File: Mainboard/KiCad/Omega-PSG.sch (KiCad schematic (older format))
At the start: 14 parts, among them J7 JOYSTICK_A, J8 JOYSTICK_B, U28 74HCT157, U29 74HCT157, U35 74HCT74, U36 74HCT74, U39 74AHCT32, U4 YM2149, U42 74LS07, U44 74AHCT02

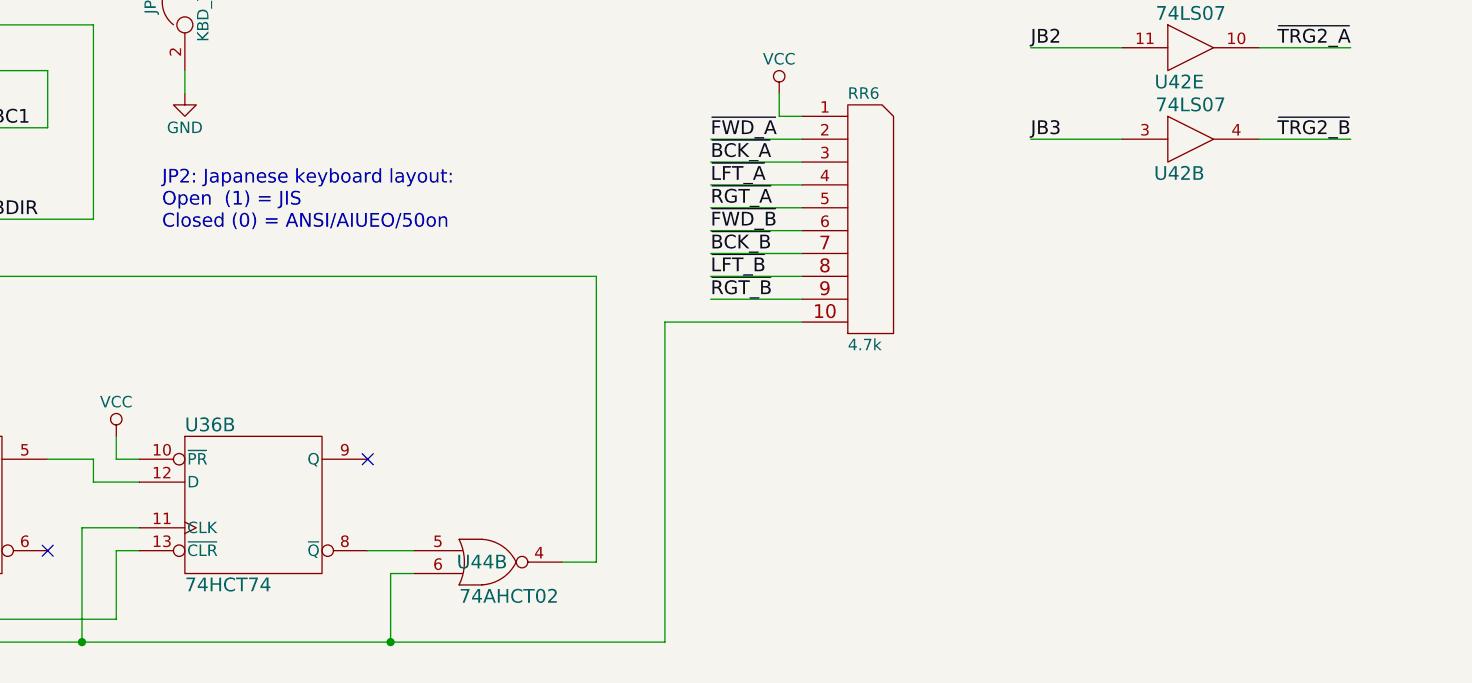
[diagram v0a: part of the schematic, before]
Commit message: Mainboard: Update to version 1.0
Signed-off-by: Sergey Kiselev <skiselev@gmail.com>
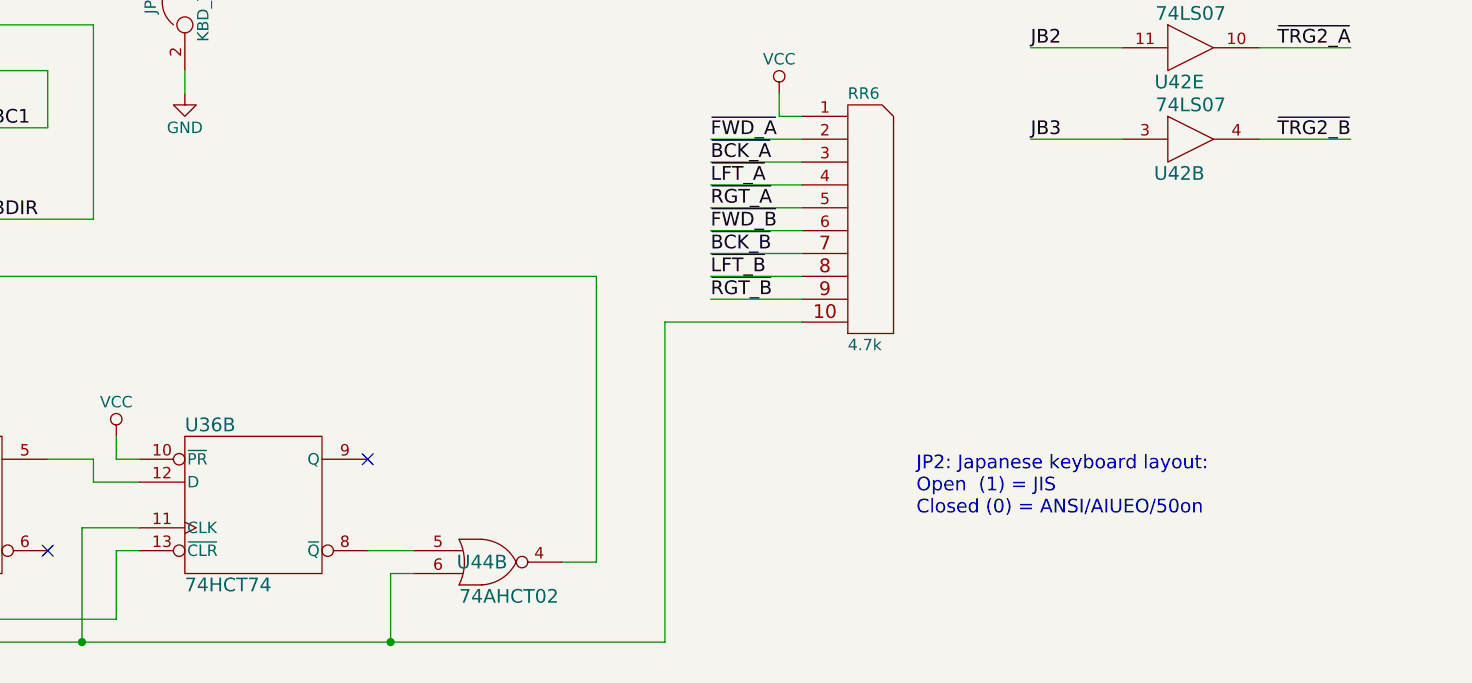
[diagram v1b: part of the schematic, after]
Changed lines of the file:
@@
 	1    0    0    -1
 $EndComp
-Text Notes 3700 5600 0    60   ~ 0
+Text Notes 7000 6850 0    60   ~ 0
 JP2: Japanese keyboard layout:\nOpen  (1) = JIS\nClosed (0) = ANSI/AIUEO/50on
 $Comp

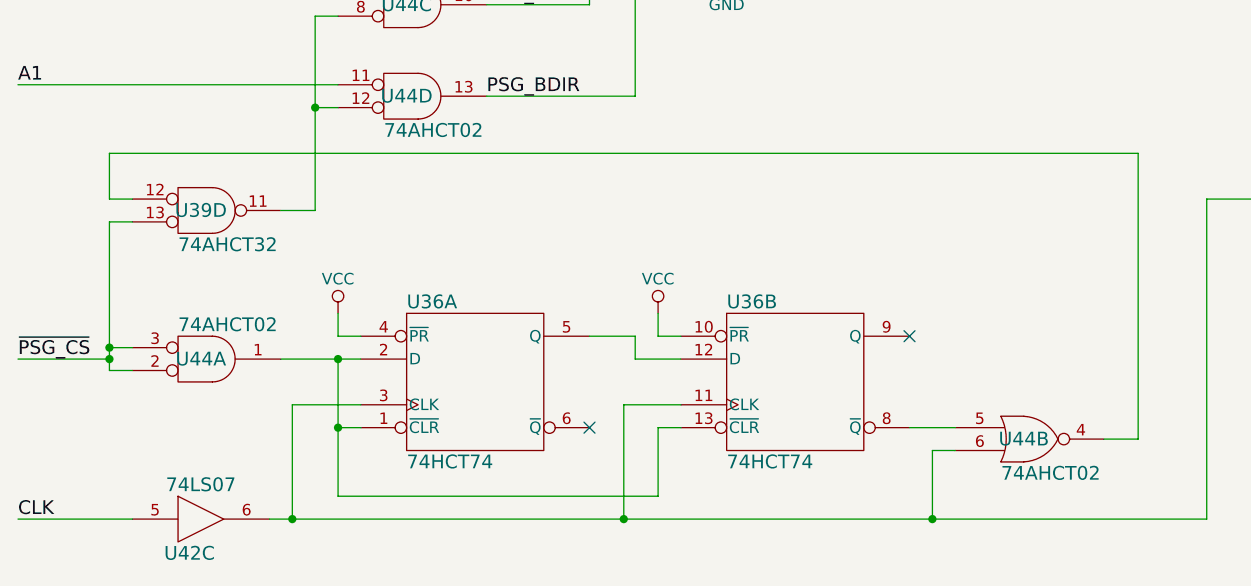
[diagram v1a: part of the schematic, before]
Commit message: Mainboard: Fix the issues discovered so far
Signed-off-by: Sergey Kiselev <skiselev@gmail.com>
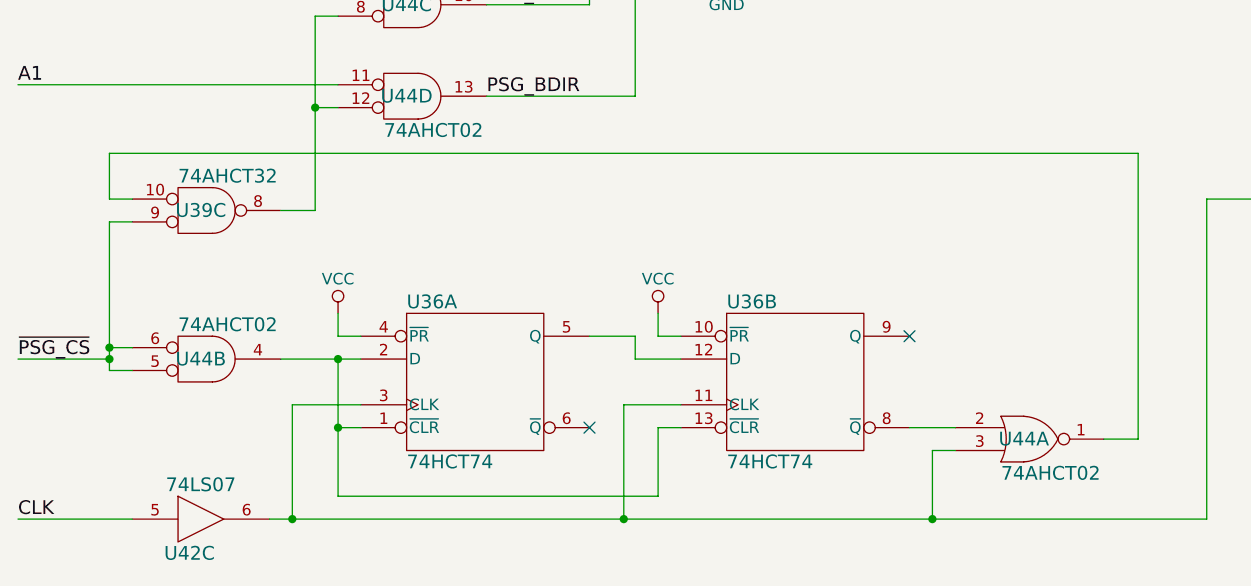
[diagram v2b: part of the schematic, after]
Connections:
- net ~PSG_CS: now also U39.9, U44.5, U44.6; no longer U39.13, U44.2, U44.3
- net at RR6.10, U36.11 (CLK), U36.3 (CLK)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: now also U44.3; no longer U44.6
- net at U36.1 (~CLR), U36.13 (~CLR), U36.2 (D): now also U44.4; no longer U44.1
- net at U36.8 (~Q): now also U44.2; no longer U44.5
- net at U44.12, U44.8: now also U39.8; no longer U39.11
- new net: U39.10, U44.1
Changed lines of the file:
@@
-$Comp
-L my_components:74LS02 U44
-U 1 2 5BEE2967
-P 1500 6700
-F 0 "U44" H 1500 6700 60  0000 C CNN
-F 1 "74AHCT02" H 1400 6550 60  0000 L CNN
-F 2 "My_Components:IC_DIP14_300" H 1500 6700 60  0001 C CNN
-F 3 "" H 1500 6700 60  0000 C CNN
-	1    1500 6700
-	1    0    0    1
-$EndComp
 $Comp
 L my_components:74LS02 U44
@@
 $Comp
 L my_components:74LS32 U39
-U 4 2 5BEE2DED
+U 3 2 5BEE2DED
 P 1500 6050
 F 0 "U39" H 1500 6050 60  0000 C CNN
@@
 F 2 "My_Components:IC_DIP14_300" H 1500 6050 60  0001 C CNN
 F 3 "" H 1500 6050 60  0000 C CNN
-	4    1500 6050
-	1    0    0    -1
+	3    1500 6050
+	1    0    0    1
 $EndComp
 Text Label 700  6700 0    60   ~ 0
@@
 Text HLabel 9500 700  2    60   Input ~ 0
 A0
-$Comp
-L my_components:74LS02 U44
-U 2 1 5BF3B597
-P 5100 7050
-F 0 "U44" H 5100 7050 60  0000 C CNN
-F 1 "74AHCT02" H 5000 6900 60  0000 L CNN
-F 2 "My_Components:IC_DIP14_300" H 5100 7050 60  0001 C CNN
-F 3 "" H 5100 7050 60  0000 C CNN
-	2    5100 7050
-	1    0    0    -1
-$EndComp
 $Comp
 L Device:R R29
@@
 Wire Wire Line
 	4700 7400 5900 7400
+$Comp
+L my_components:74LS02 U44
+U 2 2 5BEE2967
+P 1500 6700
+F 0 "U44" H 1500 6700 60  0000 C CNN
+F 1 "74AHCT02" H 1400 6550 60  0000 L CNN
+F 2 "My_Components:IC_DIP14_300" H 1500 6700 60  0001 C CNN
+F 3 "" H 1500 6700 60  0000 C CNN
+	2    1500 6700
+	1    0    0    1
+$EndComp
+$Comp
+L my_components:74LS02 U44
+U 1 1 5BF3B597
+P 5100 7050
+F 0 "U44" H 5100 7050 60  0000 C CNN
+F 1 "74AHCT02" H 5000 6900 60  0000 L CNN
+F 2 "My_Components:IC_DIP14_300" H 5100 7050 60  0001 C CNN
+F 3 "" H 5100 7050 60  0000 C CNN
+	1    5100 7050
+	1    0    0    -1
+$EndComp
 $EndSCHEMATC

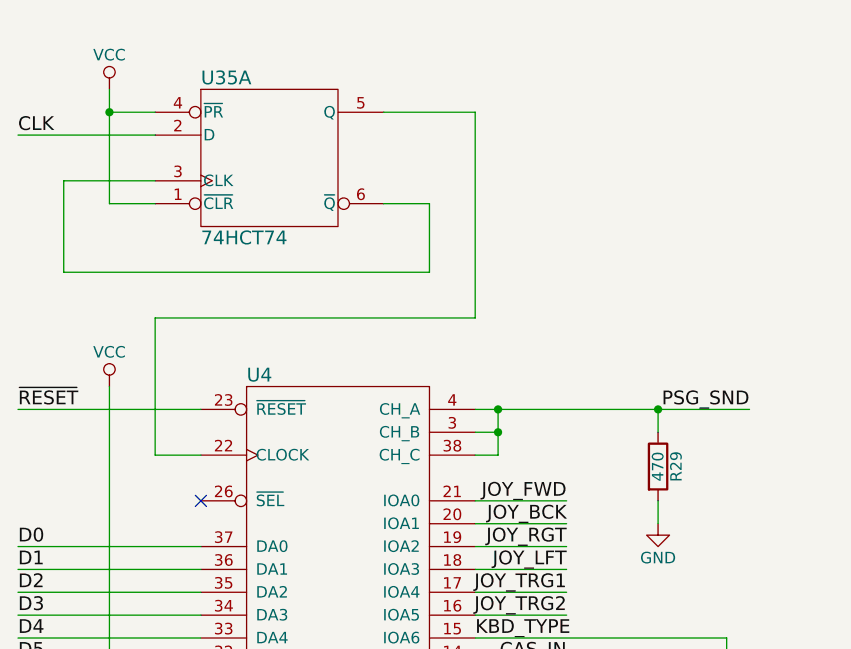
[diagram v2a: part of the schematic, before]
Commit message: Mainboard: Fixed schematic and PCB for v1.1
Signed-off-by: Sergey Kiselev <skiselev@gmail.com>
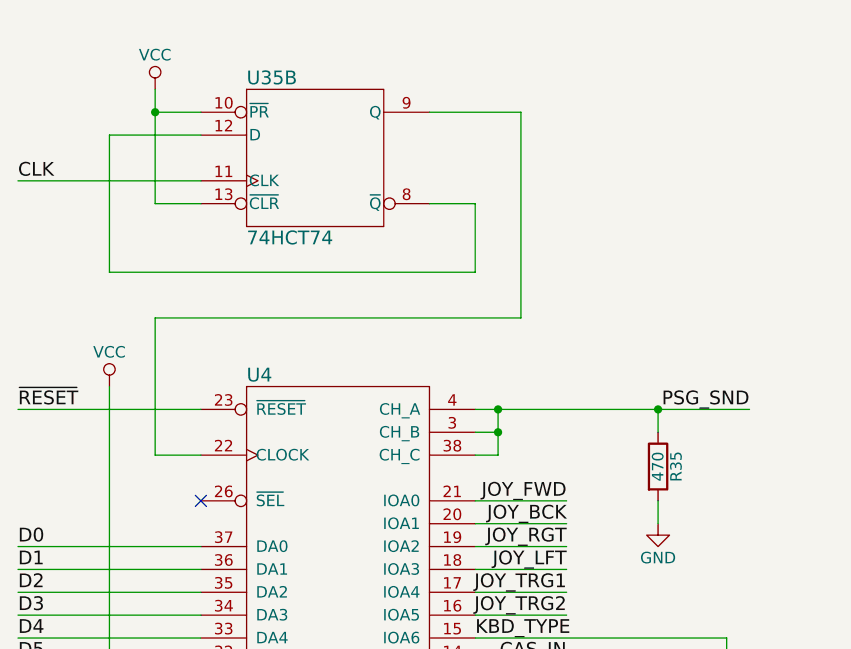
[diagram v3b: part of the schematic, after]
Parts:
- renumbered R29 to R35
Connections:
- net CLK: now also U35.11 (CLK); no longer U35.2 (D)
- net VCC: now also U35.10 (~PR), U35.13 (~CLR); no longer U35.1 (~CLR), U35.4 (~PR)
- net at U4.22 (CLOCK): now also U35.9 (Q); no longer U35.5 (Q)
- new net: U35.12 (D), U35.8 (~Q)
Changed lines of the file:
@@
 $Comp
 L my_components:74LS74 U35
-U 1 1 5BDA4A3E
-P 1800 1200
-F 0 "U35" H 1500 1550 60  0000 L CNN
-F 1 "74HCT74" H 1500 850 60  0000 L CNN
-F 2 "My_Components:IC_DIP14_300" H 1800 1200 60  0001 C CNN
-F 3 "" H 1800 1200 60  0000 C CNN
-	1    1800 1200
+U 2 1 5BDA4A3E
+P 2000 1200
+F 0 "U35" H 1700 1550 60  0000 L CNN
+F 1 "74HCT74" H 1700 850 60  0000 L CNN
+F 2 "My_Components:IC_DIP14_300" H 2000 1200 60  0001 C CNN
+F 3 "" H 2000 1200 60  0000 C CNN
+	2    2000 1200
 	1    0    0    -1
 $EndComp
@@
 L power:VCC #PWR049
 U 1 1 5BDA4C95
-P 1100 900
-F 0 "#PWR049" H 1100 750 50  0001 C CNN
-F 1 "VCC" H 1100 1050 50  0000 C CNN
-F 2 "" H 1100 900 50  0001 C CNN
-F 3 "" H 1100 900 50  0001 C CNN
-	1    1100 900
+P 1300 900
+F 0 "#PWR049" H 1300 750 50  0001 C CNN
+F 1 "VCC" H 1300 1050 50  0000 C CNN
+F 2 "" H 1300 900 50  0001 C CNN
+F 3 "" H 1300 900 50  0001 C CNN
+	1    1300 900
 	1    0    0    -1
 $EndComp
@@
 Text Label 2750 5550 0    60   ~ 0
 PSG_BDIR
-Text Label 700  1100 0    60   ~ 0
+Text Label 700  1300 0    60   ~ 0
 CLK
 Text Label 10200 700  0    60   ~ 0
@@
 A0
 $Comp
-L Device:R R29
+L Device:R R35
 U 1 1 5BF6213A
 P 3500 2550
-F 0 "R29" V 3580 2550 50  0000 C CNN
+F 0 "R35" V 3580 2550 50  0000 C CNN
 F 1 "470" V 3500 2550 50  0000 C CNN
 F 2 "My_Components:Res_762" V 3430 2550 50  0001 C CNN
@@
 Connection ~ 1100 3800
 Wire Wire Line
-	1100 1400 1300 1400
-Wire Wire Line
-	1100 900  1100 1000
-Wire Wire Line
-	1300 1000 1100 1000
-Connection ~ 1100 1000
-Wire Wire Line
-	1300 1300 900  1300
-Wire Wire Line
-	900  1300 900  1700
-Wire Wire Line
-	900  1700 2500 1700
-Wire Wire Line
-	2500 1700 2500 1400
-Wire Wire Line
-	2500 1400 2300 1400
-Wire Wire Line
-	2300 1000 2700 1000
-Wire Wire Line
-	1300 1100 700  1100
+	1300 1400 1500 1400
+Wire Wire Line
+	1300 900  1300 1000
+Wire Wire Line
+	1500 1000 1300 1000
+Connection ~ 1300 1000
+Wire Wire Line
+	1100 1100 1100 1700
+Wire Wire Line
+	1100 1700 2700 1700
+Wire Wire Line
+	2700 1700 2700 1400
+Wire Wire Line
+	2700 1400 2500 1400
+Wire Wire Line
+	2500 1000 2900 1000
+Wire Wire Line
+	1500 1300 700  1300
 Wire Wire Line
 	1500 4100 900  4100
@@
 	1300 2500 1300 1900
 Wire Wire Line
-	1300 1900 2700 1900
-Wire Wire Line
-	2700 1900 2700 1000
+	1300 1900 2900 1900
+Wire Wire Line
+	2900 1900 2900 1000
 Wire Wire Line
 	1500 3900 1300 3900
@@
 	1100 3800 1100 4200
 Wire Wire Line
-	1100 1000 1100 1400
+	1300 1000 1300 1400
 Wire Wire Line
 	3800 4200 3800 4300
@@
 	1    0    0    -1
 $EndComp
+Wire Wire Line
+	1500 1100 1100 1100
 $EndSCHEMATC
